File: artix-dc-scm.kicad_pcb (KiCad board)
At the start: 8 copper layers, 90 x 120.4 mm, 468 parts, among them IC1 TPS54561, IC2 TLV73312PDBVT, J1 L834-1G1T-S7, J12 S2B-PH-K-S_LF__SN_, J13 62000311121, J2 1-2199230-6, J3 543630489, J4 M20-7830642, J5 SFF-TA-1002-4C+, J6 0878311420, J7 61300611121, Q1 IRLML6402TRPBF, Q10 2N7002, Q11 2N7002, Q12 2N7002, Q13 2N7002, Q14 2N7002, Q15 2N7002, Q16 2N7002, Q2 IRLML6402TRPBF, Q3 IRLML6402TRPBF, Q4 IRLML6402TRPBF, Q5 IRLML6402TRPBF, Q6 IRLML6402TRPBF, Q7 2N7002, Q8 2N7002, Q9 2N7002, U1 MTFC16GAPALNA-AIT, U10 TPS62823DLCT, U11 TPS62823DLCT, U12 TPS62823DLCT, U13 TPS62823DLCT, U14 XC7A100T-FGG484, U15 SN74LVC1G08DCKR, U16 SN74LS08DBR, U17 USB3300-EZK-TR, U18 USB3300-EZK-TR, U2 W25Q32JVSSIQ_TR, U20 KSZ9031RNXCA, U3 W25Q32JVSSIQ_TR, U4 W25Q32JVSSIQ_TR, U5 W25Q32JVSSIQ_TR, U6 NVT2008DQ,115, U7 AS4C256M16D3, U8 TPS51200DRC, U9 LM3881MME_NOPB, Y1 TSX-3225, Y2 ABM8G-25.000MHZ-18-D2Y-T, Y3 TSX-3225

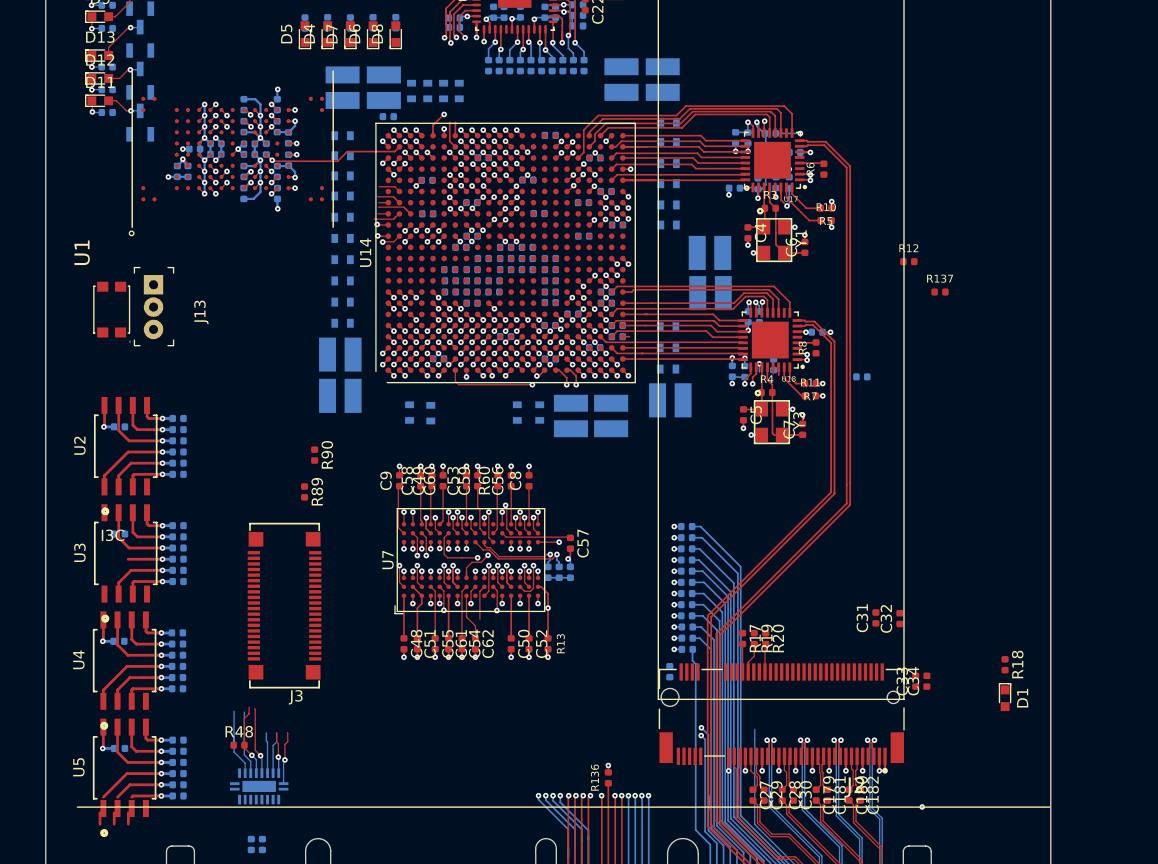
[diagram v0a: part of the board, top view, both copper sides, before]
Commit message: Reconnect eMMC, route low speed signals
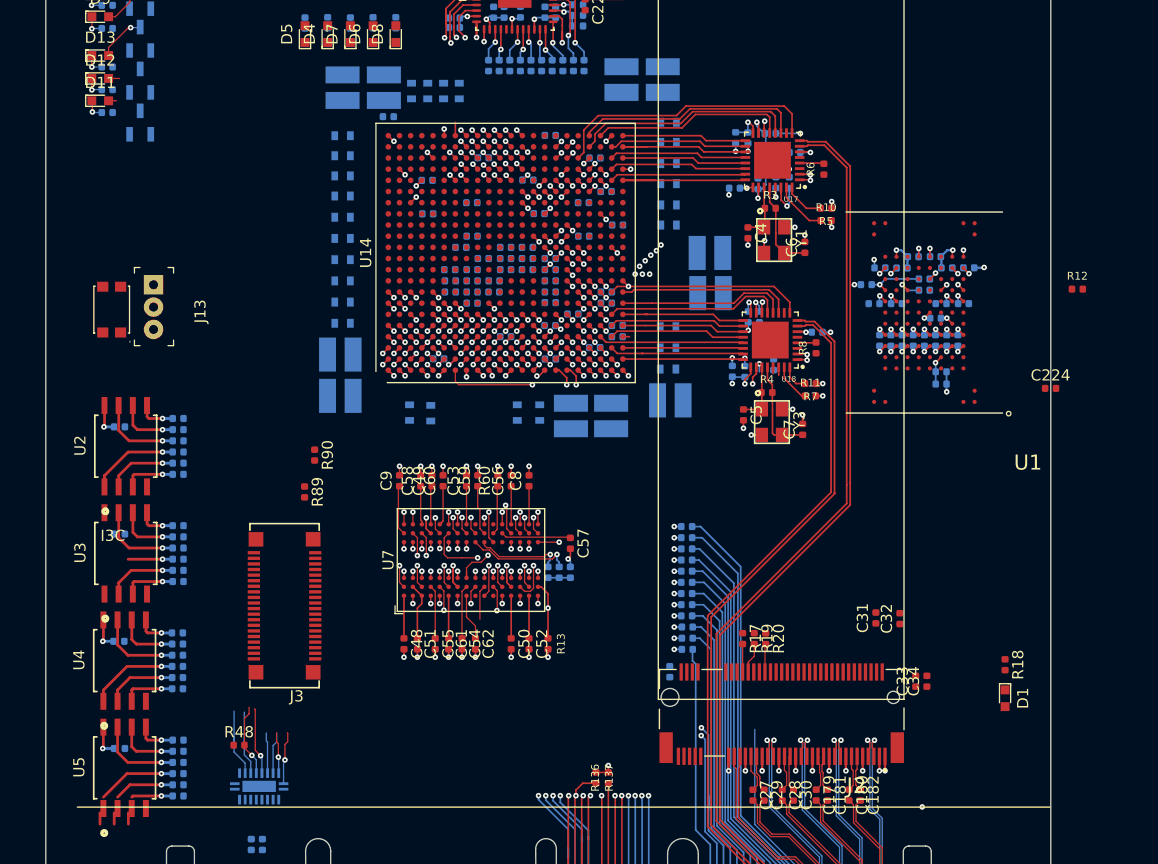
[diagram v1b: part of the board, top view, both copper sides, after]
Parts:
- added C223: C_100n_0402, artix-dc-scm-footprints:0402-cap, B.Cu at (138.8, 127.5)
- added C224: C_100n_0402, artix-dc-scm-footprints:0402-cap, F.Cu at (150.1, 131.8)
- added C229: C_100n_0402, artix-dc-scm-footprints:0402-cap, B.Cu at (139.8, 127.5)
- added C230: C_100n_0402, artix-dc-scm-footprints:0402-cap, B.Cu at (137.8, 127.5)
- added C231: C_100n_0402, artix-dc-scm-footprints:0402-cap, B.Cu at (141.8, 127.5)
- added C232: C_100n_0402, artix-dc-scm-footprints:0402-cap, B.Cu at (140.8, 127.5)
- moved C189 71.0 mm to (140.3, 131.4), turned to 0 degrees
- moved C188 69.8 mm to (140.3, 130.3), turned to 0 degrees
- moved C184 65.6 mm to (136.8, 127.5), turned to 90 degrees
- moved R119 65.2 mm to (142.3, 124.2), turned to 180 degrees
- moved U1 63.6 mm to (138.8, 125.0), turned to 180 degrees
- moved R121 63.5 mm to (140.3, 124.2), turned to 0 degrees
- moved C186 62.7 mm to (135.8, 127.5), turned to 90 degrees
- moved R120 62.3 mm to (142.8, 121.0), turned to 180 degrees
- moved C183 62.0 mm to (134.8, 127.5), turned to 90 degrees
- moved C185 61.8 mm to (138.8, 123.0), turned to 0 degrees
- moved R122 60.6 mm to (140.8, 121.0), turned to 0 degrees
- moved R124 60.5 mm to (136.3, 124.2), turned to 180 degrees
- moved R117 60.1 mm to (138.8, 122.0), turned to 0 degrees
- moved R126 59.2 mm to (134.3, 124.2), turned to 0 degrees
- moved R118 58.6 mm to (139.8, 120.0), turned to 180 degrees
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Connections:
- net GPX_USB2 renamed Net-(U14-PadB17)
- net MISO_USB2 renamed Net-(U14-PadA16)
- net MOSI_USB2 renamed Net-(U14-PadB16)
- net RST_USB2 renamed Net-(U14-PadB15)
- net SCK_USB2 renamed Net-(U14-PadA15)
- net SS_USB2 renamed Net-(U14-PadC15)
- net USB1_D0 renamed Net-(U14-PadF13)
- net USB1_D1 renamed Net-(U14-PadE14)
- net USB1_D2 renamed Net-(U14-PadE13)
- net USB1_D3 renamed Net-(U14-PadA13)
- net USB1_D4 renamed Net-(U14-PadF14)
- net USB1_D5 renamed Net-(U14-PadC13)
- net USB1_D6 renamed Net-(U14-PadB13)
- net USB1_D7 renamed Net-(U14-PadD14)
- net USB1_WR renamed Net-(U14-PadA14)
- net USB1_~RD renamed Net-(U14-PadC14)
- U14 pad A19: MMC_DAT1 -> Net-(U14-PadA19)
- U14 pad A20: MMC_DAT0 -> Net-(U14-PadA20)
- U14 pad A21: MMC_DAT5 -> Net-(U14-PadA21)
- U14 pad AA16: ESPI_IO1 -> Net-(U14-PadAA16)
- U14 pad AB13: ESPI_CLK -> Net-(U14-PadAB13)
- U14 pad AB15: ESPI_IO0 -> Net-(U14-PadAB15)
- U14 pad AB16: ESPI_CS0_N -> Net-(U14-PadAB16)
- U14 pad AB17: ESPI_CS1_N -> Net-(U14-PadAB17)
- U14 pad B20: MMC_DAT3 -> Net-(U14-PadB20)
- U14 pad B21: MMC_RSTN -> Net-(U14-PadB21)
- U14 pad B22: MMC_DAT4 -> Net-(U14-PadB22)
- U14 pad C20: MMC_CMD -> Net-(U14-PadC20)
- U14 pad C22: MMC_DAT6 -> Net-(U14-PadC22)
- U14 pad D20: MMC_DAT2 -> Net-(U14-PadD20)
- U14 pad D21: MMC_CLK -> Net-(U14-PadD21)
- U14 pad D22: MMC_DAT7 -> Net-(U14-PadD22)
- U14 pad G15: I2C[12]_SDA -> Net-(U14-PadG15)
- U14 pad G16: I2C[11]_SDA -> Net-(U14-PadG16)
- U14 pad G17: I2C[12]_SCL -> Net-(U14-PadG17)
- U14 pad H15: I2C[10]_SDA -> Net-(U14-PadH15)
- U14 pad H17: I2C[11]_SCL -> Net-(U14-PadH17)
- U14 pad H19: SGPIO1_LD -> Net-(U14-PadH19)
- U14 pad J15: I2C[9]_SDA -> Net-(U14-PadJ15)
- U14 pad J19: SGPIO1_DI -> Net-(U14-PadJ19)
- U14 pad K13: SGPIO0_CLK -> Net-(U14-PadK13)
- U14 pad K18: RSVD2 -> Net-(U14-PadK18)
- U14 pad K19: SGPIO1_DO -> Net-(U14-PadK19)
- U14 pad L18: SGPIO0_LD -> Net-(U14-PadL18)
- U14 pad L19: SGPIO0_DI -> Net-(U14-PadL19)
- U14 pad P17: Net-(U14-PadP17) -> MMC_DAT0
- U14 pad R17: Net-(U14-PadR17) -> MMC_DAT7
- U14 pad R18: Net-(U14-PadR18) -> MMC_DAT2
- U14 pad T18: Net-(U14-PadT18) -> MMC_DAT6
- U14 pad T5: Net-(U14-PadT5) -> I2C[9]_SCL
- U14 pad T6: Net-(U14-PadT6) -> I2C[9]_SDA
- U14 pad U17: Net-(U14-PadU17) -> MMC_DAT5
- U14 pad U18: Net-(U14-PadU18) -> MMC_DAT4
- U14 pad U6: Net-(U14-PadU6) -> I2C[10]_SCL
- U14 pad V18: Net-(U14-PadV18) -> MMC_DAT3
- U14 pad V19: Net-(U14-PadV19) -> MMC_RSTN
- U14 pad V5: Net-(U14-PadV5) -> SGPIO0_DO
- U14 pad V7: Net-(U14-PadV7) -> SGPIO0_LD
- U14 pad V8: Net-(U14-PadV8) -> I2C[12]_SCL
- U14 pad V9: Net-(U14-PadV9) -> I2C[12]_SDA
- U14 pad W14: ESPI_RESET_N -> Net-(U14-PadW14)
- U14 pad W17: Net-(U14-PadW17) -> MMC_DAT1
- U14 pad W4: Net-(U14-PadW4) -> SGPIO0_DI
- U14 pad W5: Net-(U14-PadW5) -> SGPIO0_CLK
- U14 pad W6: Net-(U14-PadW6) -> I2C[10]_SDA
- U14 pad W7: Net-(U14-PadW7) -> I2C[11]_SCL
- U14 pad W9: Net-(U14-PadW9) -> I2C[11]_SDA
- U14 pad Y14: ESPI_ALERT_N -> Net-(U14-PadY14)
- U14 pad Y16: ESPI_IO2 -> Net-(U14-PadY16)
- U14 pad Y17: ESPI_IO3 -> Net-(U14-PadY17)
- U14 pad Y18: Net-(U14-PadY18) -> MMC_CLK
- U14 pad Y19: Net-(U14-PadY19) -> MMC_CMD
- U14 pad Y6: Net-(U14-PadY6) -> SGPIO1_DO
- U14 pad Y7: Net-(U14-PadY7) -> RSVD2
- U14 pad Y8: Net-(U14-PadY8) -> SGPIO1_DI
- U14 pad Y9: Net-(U14-PadY9) -> SGPIO1_LD
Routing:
- net MMC_DAT0: track 15.6 -> 44.8 mm
- net MMC_DAT2: track 17.9 -> 44.8 mm
- net MMC_RSTN: track 13.5 -> 39.4 mm, vias 1 -> 2
- net MMC_DAT3: track 14.5 -> 40.0 mm
- net MMC_DAT1: track 15.2 -> 40.1 mm
- net MMC_CMD: track 12.5 -> 35.1 mm
- net MMC_DAT4: track 14.3 -> 35.4 mm
- net MMC_DAT5: track 15.2 -> 35.9 mm
- net MMC_DAT6: track 15.9 -> 35.6 mm
- net MMC_CLK: track 15.2 -> 33.7 mm
- net MMC_DAT7: track 17.3 -> 35.6 mm
- net VCC3V3: track 91.6 -> 74.3 mm, vias 36 -> 35
- net JTAG_TDI: track 0.00 -> 10.2 mm, vias 0 -> 2
- net JTAG_TMS: track 0.00 -> 10.2 mm, vias 0 -> 2
- net JTAG_TDO: track 0.00 -> 9.54 mm, vias 0 -> 2
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
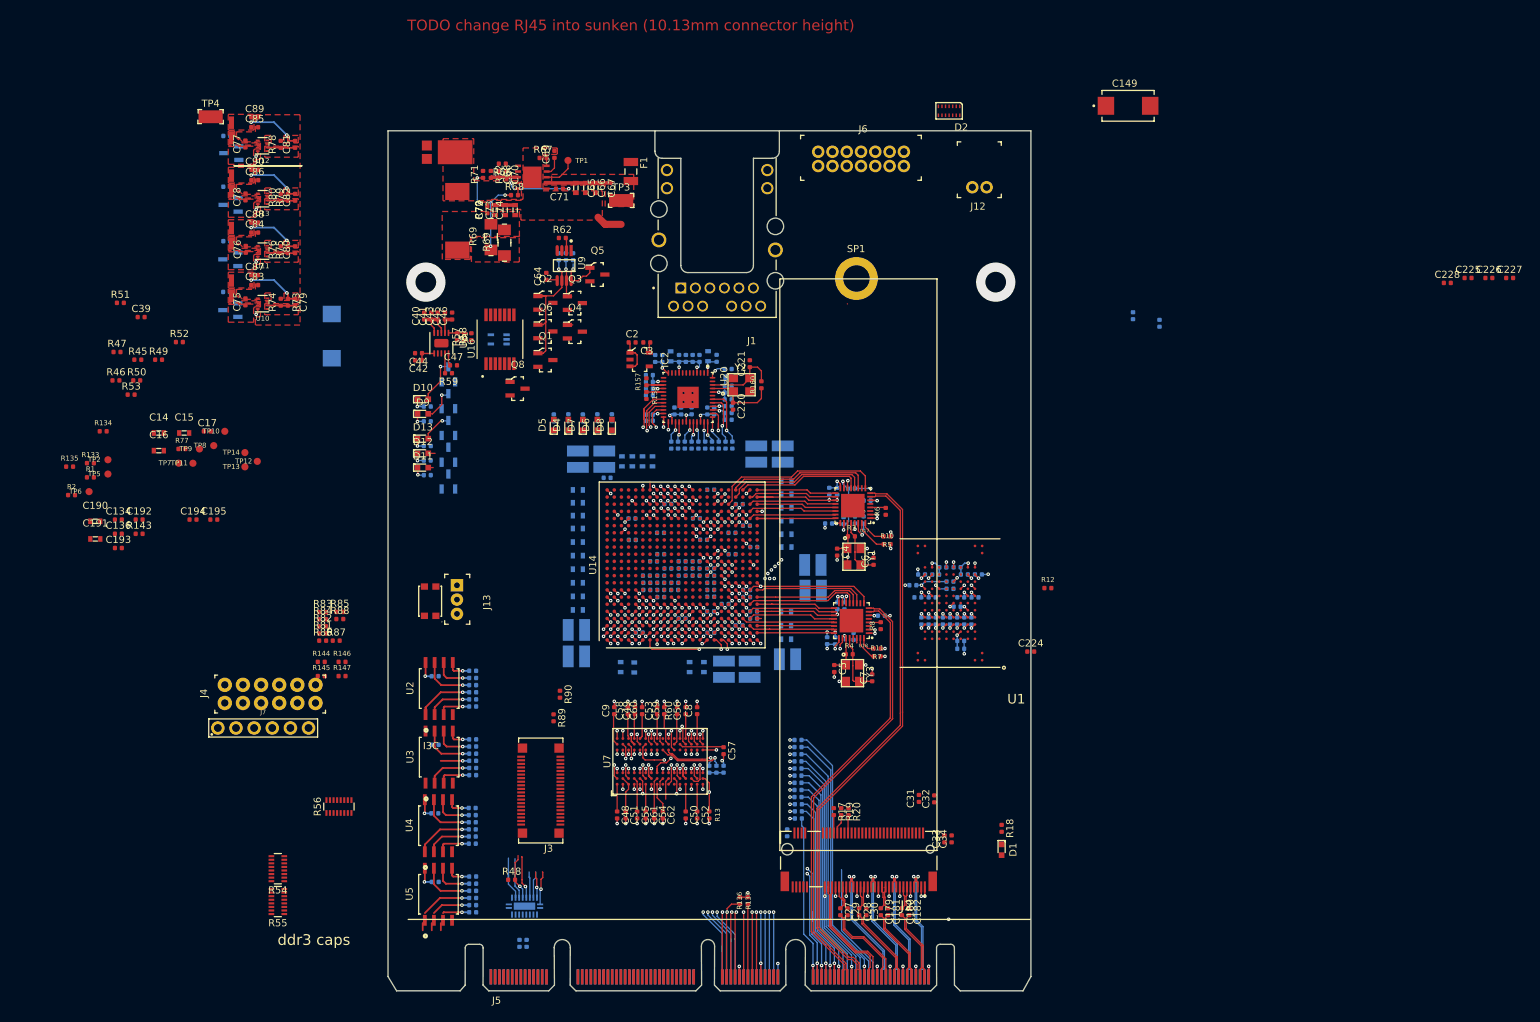
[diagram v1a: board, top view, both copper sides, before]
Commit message: Route BMC PCIe
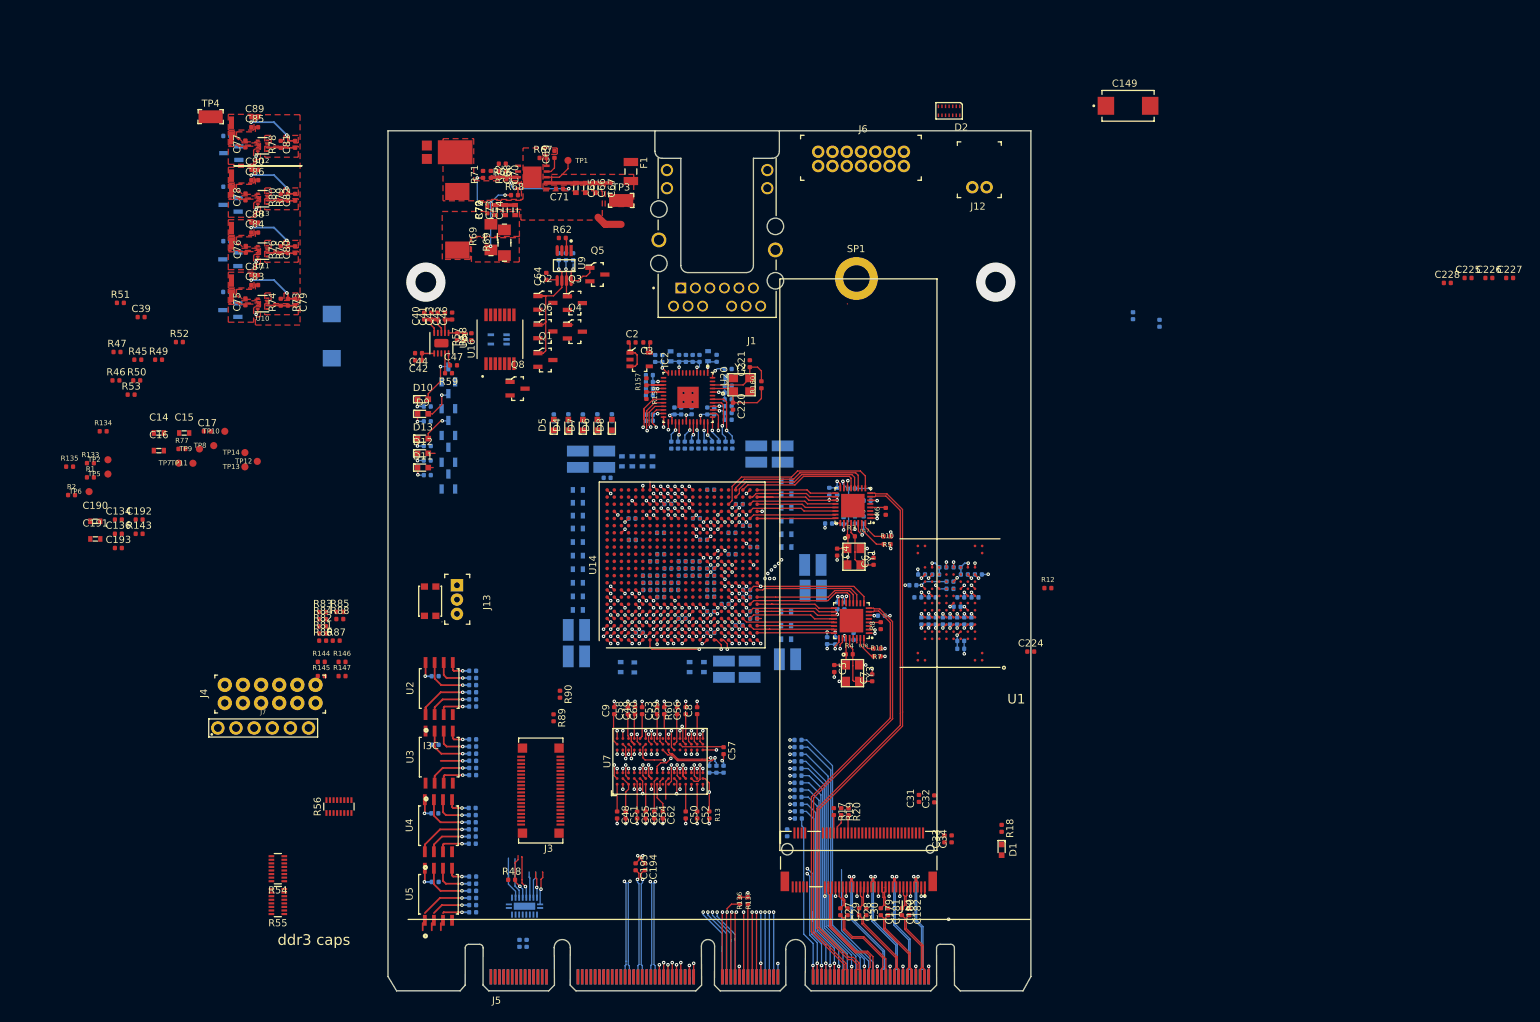
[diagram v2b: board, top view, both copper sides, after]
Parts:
- moved C194 79.8 mm to (96.1, 161.9), turned to 270 degrees
- moved C195 76.5 mm to (94.8, 161.9), turned to 270 degrees
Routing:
- net PCIE_BMC_CLK_100_P: track 0.71 -> 64.2 mm, vias 1 -> 2
- net PCIE_BMC_CLK_100_N: track 0.71 -> 63.8 mm, vias 1 -> 2
- net PCIE_BMC_RX_P: track 0.71 -> 62.7 mm, vias 1 -> 2
- net PCIE_BMC_RX_N: track 0.71 -> 62.2 mm, vias 1 -> 2
- net /Interfaces/PCIE_BMC_TX_C_P: track 0.71 -> 42.7 mm, vias 1 -> 2
- net /Interfaces/PCIE_BMC_TX_C_N: track 0.71 -> 42.1 mm, vias 1 -> 2
- net PCIE_BMC_TX_N: track 0.00 -> 15.4 mm, vias 0 -> 1
- net PCIE_BMC_TX_P: track 0.00 -> 15.4 mm, vias 0 -> 1
- net PVCCIO_PECI: track 0.00 -> 1.90 mm, vias 0 -> 1
- net NCSI_TXD0: track 0.00 -> 1.90 mm, vias 0 -> 1
- net NCSI_RXER: track 0.00 -> 1.90 mm, vias 0 -> 1
- net NCSI_RXD1: track 0.00 -> 1.90 mm, vias 0 -> 1
- net PECI_BMC: track 0.00 -> 1.60 mm, vias 0 -> 1
- net NCSI_TXEN: track 0.00 -> 1.60 mm, vias 0 -> 1
- net NCSI_TXD1: track 0.00 -> 1.60 mm, vias 0 -> 1
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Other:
- net class PCIe_inner added: clearance 0.21, trace_width 0.11, via_dia 0.5, via_drill 0.2
- board text removed: "TODO change RJ45 into sunken (10.13mm connector height)"
